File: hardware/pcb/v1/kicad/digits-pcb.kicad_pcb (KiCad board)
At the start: 2 copper layers, 76.2 x 56.9 mm, 22 parts, among them J1 Conn_02x20_Odd_Even, J10 Conn_01x02, J2 Conn_01x03, J3 Barrel_Jack_Switch, J4 Conn_01x07, J5 Conn_01x04, J6 Conn_01x02, J7 Screw_Terminal_01x02, J8 Conn_01x04, J9 Conn_01x03, SW1 SW_Push, U1 LM2596S-5

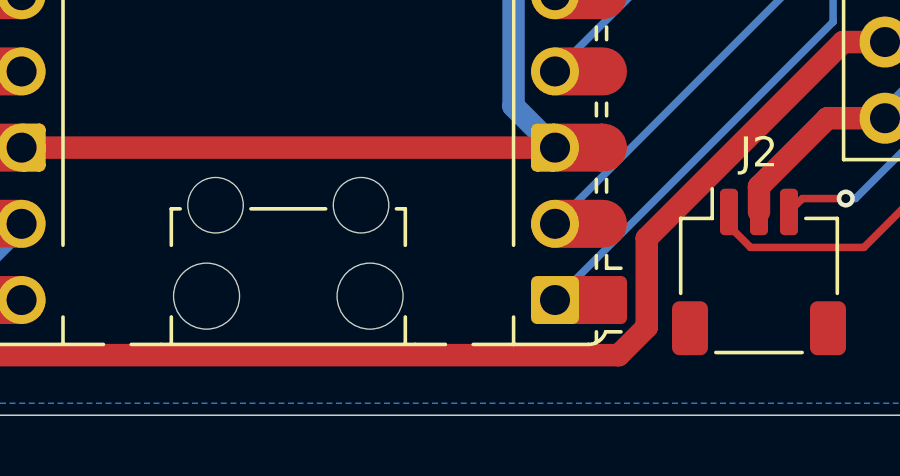
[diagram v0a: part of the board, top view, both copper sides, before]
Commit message: fix(hardware): power integrity audit + board version silkscreens
V2 (before JLCPCB resubmit):
- Add Switching netclass (0.75mm) and route SW_NODE at 0.75mm F.Cu
- Fix /VIN_RAW hierarchical pattern mismatch (was VIN_RAW)
- Add BELL_A/B and +3V3 to Power netclass patterns
- Reroute BELL_A/B at 0.4mm to survive DRV8871 ILIM fault (1.94A)
- Add thermal stitching vias (U1: 9, U2: 4, U3: 4, U6: 4) on GND
- Reconnect +5V from J1 to U1/L1 (split-net that DRC did not flag)
- Add custom DRC rules (.kicad_dru) to catch future netclass regressions
- Silkscreen: "Digits V2" on F.Silkscreen
- ERRATA.md documenting fixes and outstanding power integrity audit

V1 (forward fix for errata #1 switching node undersized):
- Label switching node as VSW in schematic
- Add VSW to Power netclass patterns
- Silkscreen: "Digits v1.1" on F.Silkscreen

Gitignore kicad-cli DRC report artifacts.
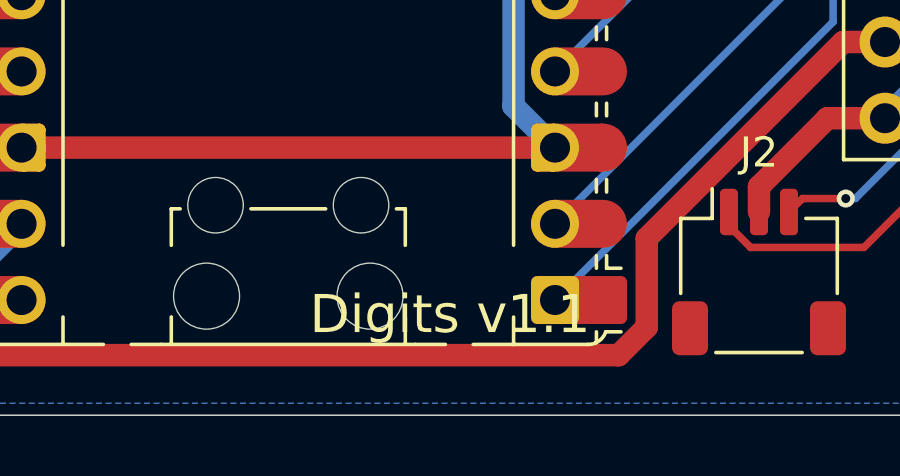
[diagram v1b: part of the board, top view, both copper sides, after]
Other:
- board text added: "Digits v1.1"
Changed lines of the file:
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@@
 		(layer "Edge.Cuts")
+	)
+	(gr_text "Digits v1.1"
+		(at 53 68 0)
+		(layer "F.SilkS")
+		(effects
+			(font
+				(size 1.27 1.27)
+				(thickness 0.15)
+			)
+		)
 	)
 	(segment

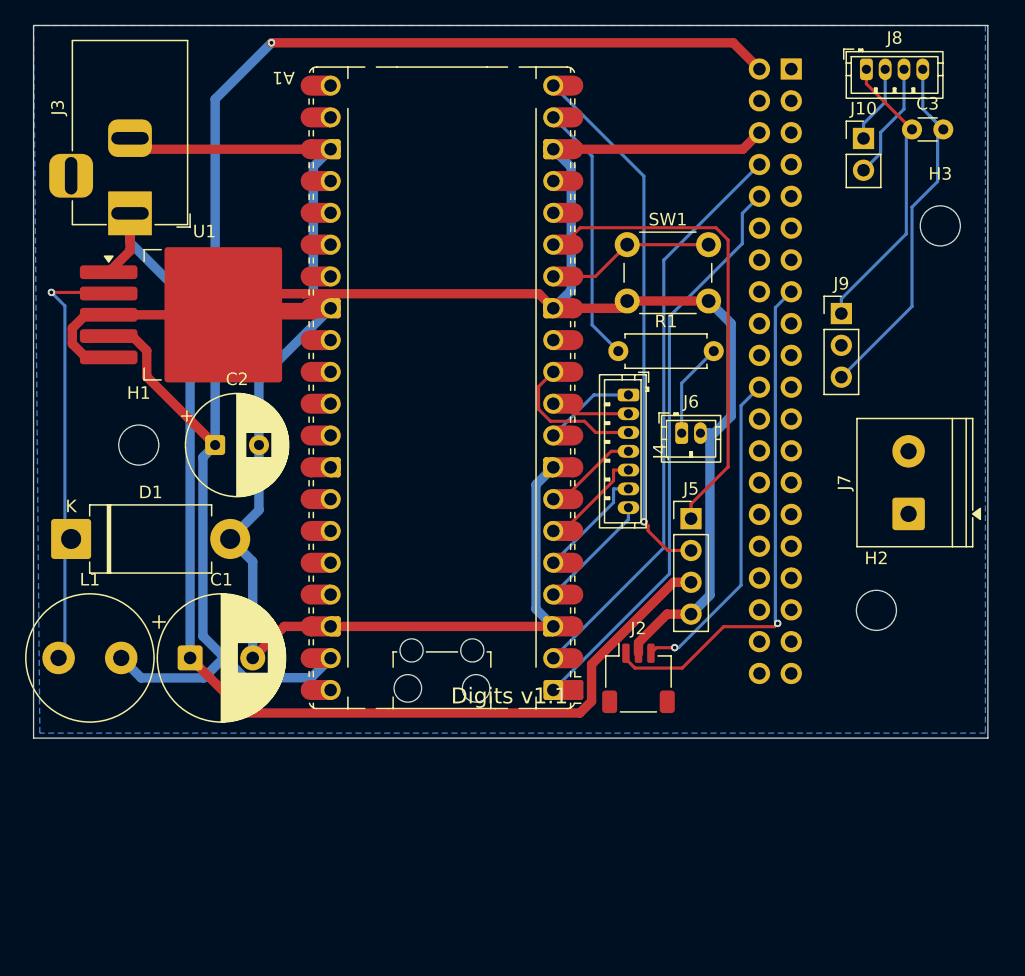
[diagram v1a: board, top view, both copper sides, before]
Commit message: feat(hardware): v1.1 design in progress — codec header + audit follow-ups
Schematic (via subagents + manual):
- Add J_CODEC (2x20 female, Conn_02x20_Odd_Even) for the Codec Zero HAT to
  plug into directly via its factory 40-pin receptacle
- Add global labels linking J1 <-> J_CODEC for the 8 audio + power signals:
  CODEC_SDA, CODEC_SCL, CODEC_BCLK, CODEC_WCLK, CODEC_DIN, CODEC_DOUT, plus
  +3V3 and GND
- Add HAT_ID_SD / HAT_ID_SC labels on J1 pins 27/28 and J_CODEC pins 27/28
  so the Pi bootloader can auto-detect the HAT via its on-board EEPROM
- No_connect flags on unused J_CODEC pins

ERRATA.md:
- Annotate v1.1 resolution status for each of the 5 pre-existing errata
  items. #1 (switching node) marked APPLIED; #2-5 marked PENDING for v1.1
- Add introductory note that the design files in this directory are now
  evolving toward v1.1

PCB (WIP):
- Initial placement tweaks; full routing of J_CODEC + resolution of the
  other errata items is in progress
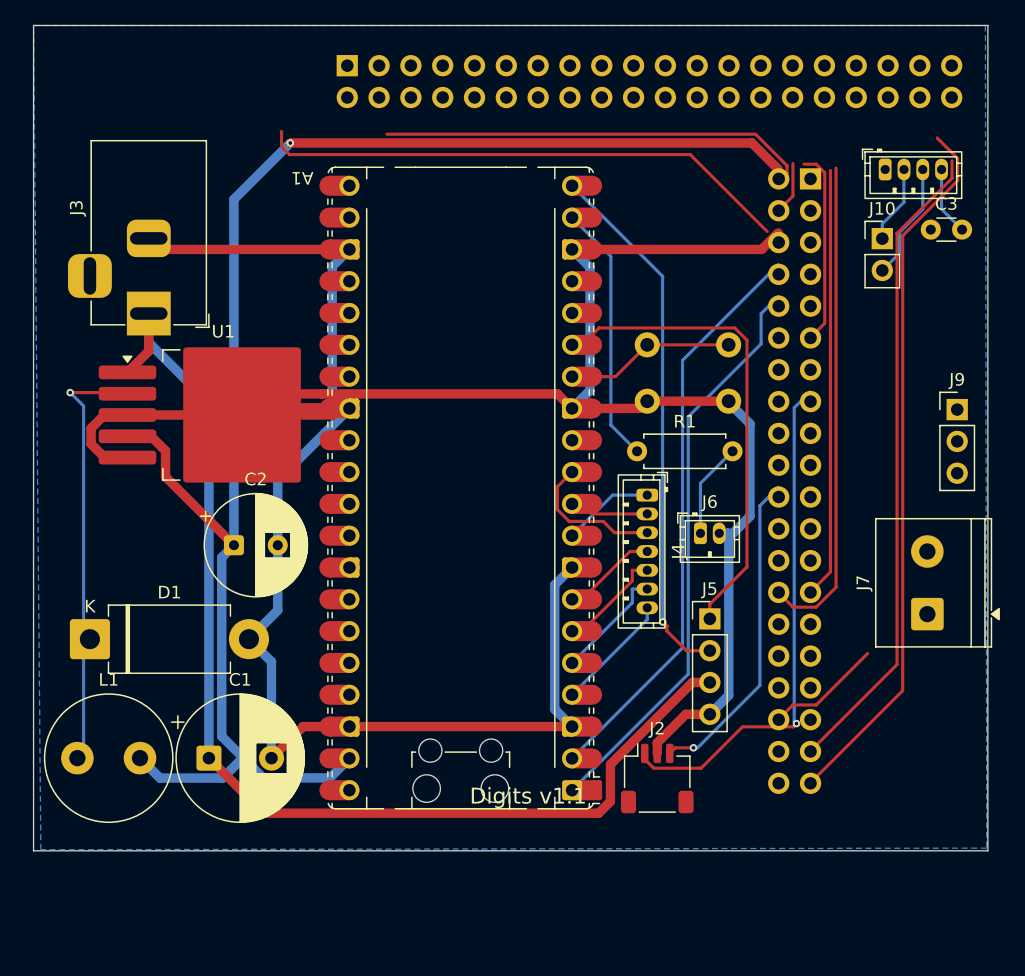
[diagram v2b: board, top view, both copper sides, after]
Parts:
- removed H1, H2, H3: MountingHole_3.2mm_M3, MountingHole:MountingHole_3.2mm_M3
- added J_CODEC1: 2x20 female header (Codec Zero), Connector_PinHeader_2.54mm:PinHeader_2x20_P2.54mm_Vertical, B.Cu at (40.0, 17.7)
- SW1: moved to B.Cu
- moved J9 12.0 mm to (88.8, 45.1)
- moved SW1 11.4 mm to (70.5, 40.0), turned to 180 degrees
- moved J1 8.90 mm to (77.0, 26.7)
- moved A1 8.14 mm to (49.1, 51.4)
- moved C1 8.14 mm to (29.0, 73.0)
- moved C2 8.14 mm to (31.0, 56.0)
- moved C3 8.14 mm to (86.6, 30.8)
- moved D1 8.14 mm to (19.5, 63.5)
- moved J10 8.14 mm to (82.8, 31.5)
- moved J2 8.14 mm to (64.8, 74.6)
- moved J3 8.14 mm to (24.2, 37.5)
- moved J4 8.14 mm to (64.0, 52.0)
- moved J5 8.14 mm to (69.0, 61.8)
- moved J6 8.14 mm to (68.2, 55.0)
- moved J7 8.14 mm to (86.4, 61.5)
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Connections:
- net Net-(D1-K) renamed /VSW
- J1 pad 1: unconnected-(J1-Pin_1-Pad1) -> +3V3
- J1 pad 12: unconnected-(J1-Pin_12-Pad12) -> CODEC_BCLK
- J1 pad 27: unconnected-(J1-Pin_27-Pad27) -> HAT_ID_SD
- J1 pad 28: unconnected-(J1-Pin_28-Pad28) -> HAT_ID_SC
- J1 pad 3: unconnected-(J1-Pin_3-Pad3) -> CODEC_SDA
- J1 pad 35: unconnected-(J1-Pin_35-Pad35) -> CODEC_WCLK
- J1 pad 38: unconnected-(J1-Pin_38-Pad38) -> CODEC_DIN
- J1 pad 40: unconnected-(J1-Pin_40-Pad40) -> CODEC_DOUT
- J1 pad 5: unconnected-(J1-Pin_5-Pad5) -> CODEC_SCL
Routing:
- net unconnected-(J1-Pin_39-Pad39): track 0.00 -> 57.1 mm
- net unconnected-(J1-Pin_37-Pad37): track 0.00 -> 51.9 mm
- net unconnected-(J1-Pin_4-Pad4): track 0.00 -> 47.0 mm
- net HAT_ID_SC: track 0.00 -> 39.2 mm
- net +5V: track 125.4 -> 159.8 mm
- net HAT_ID_SD: track 0.00 -> 34.4 mm
- net /MIC_GND: track 29.8 -> 5.48 mm
- net /MIC_HOT: track 23.3 -> 0.00 mm
- net unconnected-(J_CODEC1-Pin_11-Pad11): track 0.00 -> 15.6 mm
- net CODEC_WCLK: track 0.00 -> 9.32 mm
- net GND: vias 0 -> 1
- net /SWD_SWDIO: vias 1 -> 0
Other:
- board size 76.2 x 56.9 mm -> 76.2 x 65.9 mm

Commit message: chore(hardware): v1.1 WIP checkpoint - codec passthrough, mic jumper, VSW
Schematic (ERC clean):
- All 40 pins of J1 (Pi) and J_CODEC (Codec Zero) tied pin-for-pin via
  global labels for full HAT-style GPIO passthrough
- Wire CODEC_MCLK on pin 7 (was missing - required for TLV320AIC3104
  master clock derived from Pi GPCLK0)
- Add J11 1x2 mic-to-codec jumper (pin 1 = MIC_FROM_SW, pin 2 = MIC_GND);
  mirrors J10 earpiece pattern. Eliminates the v1.0 flying-wire kludge
  from J9 to the Codec Zero mic JST.
- Add 3 mounting hole symbols (MH1/2/3) with markup matching v2 style
- Fix J_CODEC value/description text to read "male" header (footprint
  was always male PinHeader; only the labels were wrong)

PCB (DRC clean with --refill-zones):
- Restore mounting holes at original v1 positions; add schematic-link
  metadata (path/sheetname/sheetfile/units) so KiCad recognizes them
  as schematic-backed components
- Apply errata #1 PCB-side fix: rename Net-(D1-K) to /VSW (sheet-scoped
  label name from schematic) and widen 5 buck switching segments from
  0.25mm to 0.75mm
- Update Power netclass pattern in .kicad_pro from "VSW" to "/VSW" to
  match the slash-prefixed name (per power-integrity audit memory:
  hierarchical net path prefixes silently break unprefixed patterns)

NEXT_STEPS.md added documenting remaining work. Main blocker is
mechanical: the Pi and Codec Zero overlap in the current J1/J_CODEC
orientation. Several errata items still pending. Not ready for fab.
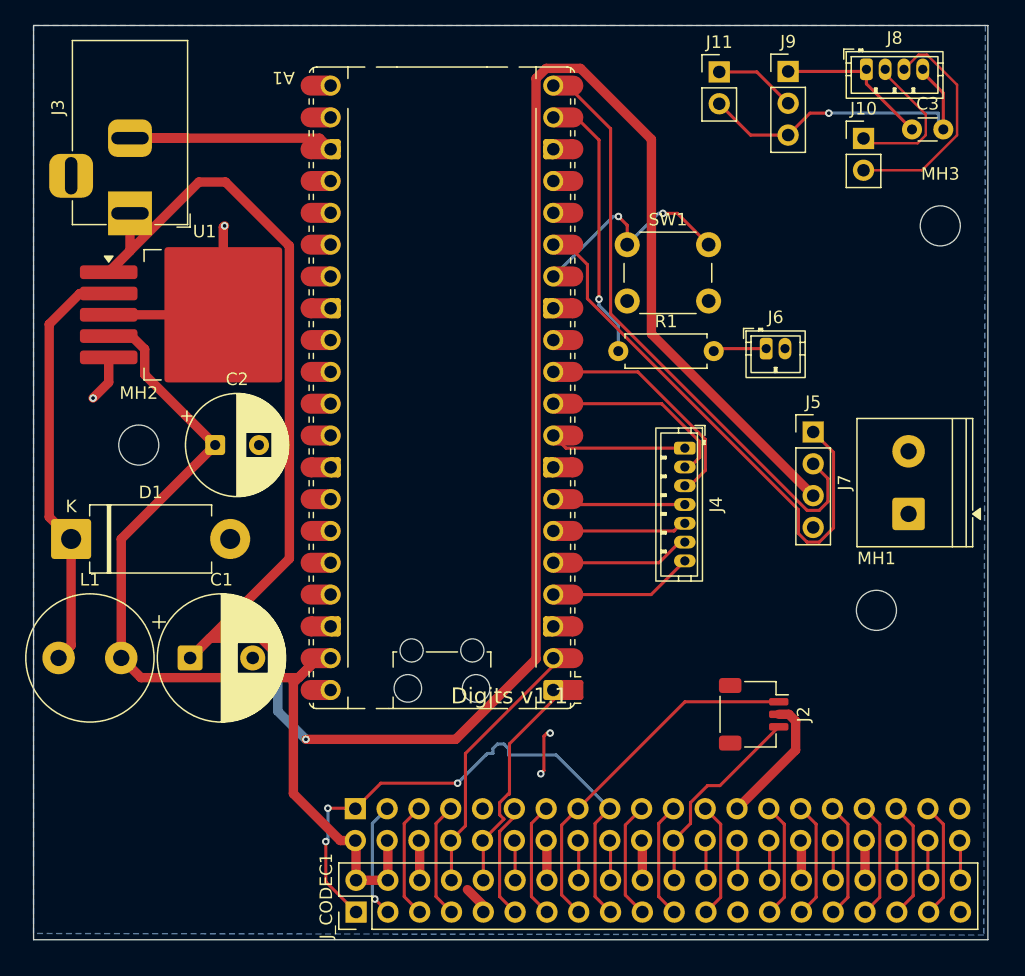
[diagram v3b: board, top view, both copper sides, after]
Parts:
- added J11: Mic Kill, Connector_PinHeader_2.54mm:PinHeader_1x02_P2.54mm_Vertical, F.Cu at (69.8, 18.2)
- added MH1: MountingHole, MountingHole:MountingHole_3.2mm_M3, F.Cu at (82.3, 61.2)
- added MH2: MountingHole, MountingHole:MountingHole_3.2mm_M3, F.Cu at (23.4, 48.0)
- added MH3: MountingHole, MountingHole:MountingHole_3.2mm_M3, F.Cu at (87.4, 30.5)
- J_CODEC1: value 2x20 female header (Codec Zero) -> 2x20 male header (Codec Zero); moved to F.Cu
- SW1: moved to F.Cu
- moved J_CODEC1 67.6 mm to (40.8, 85.2), turned to 90 degrees
- moved J1 62.1 mm to (40.7, 77.0), turned to -90 degrees
- moved J9 30.2 mm to (75.2, 18.1)
- moved J5 17.0 mm to (77.2, 46.9)
- moved J6 15.7 mm to (73.5, 40.3)
- moved SW1 11.4 mm to (62.4, 32.0), turned to 0 degrees
- moved J2 9.25 mm to (72.5, 69.5), turned to -90 degrees
- moved A1 8.14 mm to (47.6, 43.4)
- moved C1 8.14 mm to (27.5, 65.0)
- moved C2 8.14 mm to (29.5, 48.0)
- moved C3 8.14 mm to (85.1, 22.8)
- moved D1 8.14 mm to (18.0, 55.5)
- moved J10 8.14 mm to (81.3, 23.5)
- moved J3 8.14 mm to (22.7, 29.5)
- moved J7 8.14 mm to (84.9, 53.5)
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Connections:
- A1 pad 1: /UART_RX_PI -> UART_RX_PI
- A1 pad 2: /UART_TX_PI -> UART_TX_PI
- J1 pad 10: /UART_RX_PI -> UART_RX_PI
- J1 pad 11: unconnected-(J1-Pin_11-Pad11) -> PI_GPIO17
- J1 pad 13: unconnected-(J1-Pin_13-Pad13) -> PI_GPIO27
- J1 pad 14: unconnected-(J1-Pin_14-Pad14) -> GND
- J1 pad 15: /SWD_SWDIO -> SWD_SWDIO
- J1 pad 16: unconnected-(J1-Pin_16-Pad16) -> PI_GPIO23
- J1 pad 17: unconnected-(J1-Pin_17-Pad17) -> +3V3
- J1 pad 18: unconnected-(J1-Pin_18-Pad18) -> PI_GPIO24
- J1 pad 19: unconnected-(J1-Pin_19-Pad19) -> PI_GPIO10
- J1 pad 20: unconnected-(J1-Pin_20-Pad20) -> GND
- J1 pad 21: unconnected-(J1-Pin_21-Pad21) -> PI_GPIO9
- J1 pad 22: /SWD_SWCLK -> SWD_SWCLK
- J1 pad 23: unconnected-(J1-Pin_23-Pad23) -> PI_GPIO11
- J1 pad 24: unconnected-(J1-Pin_24-Pad24) -> PI_GPIO8
- J1 pad 25: unconnected-(J1-Pin_25-Pad25) -> GND
- J1 pad 26: unconnected-(J1-Pin_26-Pad26) -> PI_GPIO7
- J1 pad 29: unconnected-(J1-Pin_29-Pad29) -> PI_GPIO5
- J1 pad 30: unconnected-(J1-Pin_30-Pad30) -> GND
- J1 pad 31: unconnected-(J1-Pin_31-Pad31) -> PI_GPIO6
- J1 pad 32: unconnected-(J1-Pin_32-Pad32) -> PI_GPIO12
- J1 pad 33: unconnected-(J1-Pin_33-Pad33) -> PI_GPIO13
- J1 pad 34: unconnected-(J1-Pin_34-Pad34) -> GND
- J1 pad 36: unconnected-(J1-Pin_36-Pad36) -> PI_GPIO16
- J1 pad 37: unconnected-(J1-Pin_37-Pad37) -> PI_GPIO26
- J1 pad 39: unconnected-(J1-Pin_39-Pad39) -> GND
- J1 pad 4: unconnected-(J1-Pin_4-Pad4) -> +5V
- J1 pad 7: unconnected-(J1-Pin_7-Pad7) -> CODEC_MCLK
- J1 pad 8: /UART_TX_PI -> UART_TX_PI
- J1 pad 9: unconnected-(J1-Pin_9-Pad9) -> GND
- J2 pad 1: /SWD_SWDIO -> SWD_SWDIO
- J2 pad 3: /SWD_SWCLK -> SWD_SWCLK
- J_CODEC1 pad 10: unconnected-(J_CODEC1-Pin_10-Pad10) -> UART_RX_PI
- J_CODEC1 pad 11: unconnected-(J_CODEC1-Pin_11-Pad11) -> PI_GPIO17
- J_CODEC1 pad 13: unconnected-(J_CODEC1-Pin_13-Pad13) -> PI_GPIO27
- J_CODEC1 pad 14: unconnected-(J_CODEC1-Pin_14-Pad14) -> GND
- J_CODEC1 pad 15: unconnected-(J_CODEC1-Pin_15-Pad15) -> SWD_SWDIO
- J_CODEC1 pad 16: unconnected-(J_CODEC1-Pin_16-Pad16) -> PI_GPIO23
- J_CODEC1 pad 17: unconnected-(J_CODEC1-Pin_17-Pad17) -> +3V3
- J_CODEC1 pad 18: unconnected-(J_CODEC1-Pin_18-Pad18) -> PI_GPIO24
- J_CODEC1 pad 19: unconnected-(J_CODEC1-Pin_19-Pad19) -> PI_GPIO10
- J_CODEC1 pad 2: unconnected-(J_CODEC1-Pin_2-Pad2) -> +5V
- J_CODEC1 pad 20: unconnected-(J_CODEC1-Pin_20-Pad20) -> GND
- J_CODEC1 pad 21: unconnected-(J_CODEC1-Pin_21-Pad21) -> PI_GPIO9
- J_CODEC1 pad 22: unconnected-(J_CODEC1-Pin_22-Pad22) -> SWD_SWCLK
- J_CODEC1 pad 23: unconnected-(J_CODEC1-Pin_23-Pad23) -> PI_GPIO11
- J_CODEC1 pad 24: unconnected-(J_CODEC1-Pin_24-Pad24) -> PI_GPIO8
- J_CODEC1 pad 25: unconnected-(J_CODEC1-Pin_25-Pad25) -> GND
- J_CODEC1 pad 26: unconnected-(J_CODEC1-Pin_26-Pad26) -> PI_GPIO7
- J_CODEC1 pad 29: unconnected-(J_CODEC1-Pin_29-Pad29) -> PI_GPIO5
- J_CODEC1 pad 30: unconnected-(J_CODEC1-Pin_30-Pad30) -> GND
- J_CODEC1 pad 31: unconnected-(J_CODEC1-Pin_31-Pad31) -> PI_GPIO6
- J_CODEC1 pad 32: unconnected-(J_CODEC1-Pin_32-Pad32) -> PI_GPIO12
- J_CODEC1 pad 33: unconnected-(J_CODEC1-Pin_33-Pad33) -> PI_GPIO13
- J_CODEC1 pad 34: unconnected-(J_CODEC1-Pin_34-Pad34) -> GND
- J_CODEC1 pad 36: unconnected-(J_CODEC1-Pin_36-Pad36) -> PI_GPIO16
- J_CODEC1 pad 37: unconnected-(J_CODEC1-Pin_37-Pad37) -> PI_GPIO26
- J_CODEC1 pad 39: unconnected-(J_CODEC1-Pin_39-Pad39) -> GND
- J_CODEC1 pad 4: unconnected-(J_CODEC1-Pin_4-Pad4) -> +5V
- J_CODEC1 pad 7: unconnected-(J_CODEC1-Pin_7-Pad7) -> CODEC_MCLK
- J_CODEC1 pad 8: unconnected-(J_CODEC1-Pin_8-Pad8) -> UART_TX_PI
- J_CODEC1 pad 9: unconnected-(J_CODEC1-Pin_9-Pad9) -> GND
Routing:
- net GND: track 238.0 -> 73.5 mm, vias 1 -> 4
- net +12V: track 90.8 -> 190.0 mm, vias 0 -> 2
- net +5V: track 159.8 -> 78.7 mm, vias 1 -> 0
- net unconnected-(J1-Pin_39-Pad39): track 57.1 -> 0.00 mm
- net unconnected-(J1-Pin_37-Pad37): track 51.9 -> 0.00 mm
- net unconnected-(J1-Pin_4-Pad4): track 47.0 -> 0.00 mm
- net /UART_TX_PI: track 47.0 -> 0.00 mm
- net /UART_RX_PI: track 47.0 -> 0.00 mm
- net +3V3: track 0.00 -> 45.9 mm, vias 0 -> 3
- net /SWD_SWDIO: track 41.4 -> 0.00 mm
- net HAT_ID_SC: track 39.2 -> 3.19 mm
- net SWD_SWDIO: track 0.00 -> 28.9 mm
- net /SWD_SWCLK: track 25.9 -> 0.00 mm, vias 1 -> 0
- net HAT_ID_SD: track 34.4 -> 9.25 mm
- net UART_TX_PI: track 0.00 -> 21.6 mm
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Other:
- board size 76.2 x 65.9 mm -> 76.2 x 73 mm
